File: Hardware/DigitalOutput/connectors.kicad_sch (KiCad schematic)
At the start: 12 parts, among them J1 DIGITAL INPUT, J2 DIGITAL OUTPUT, J3 Conn_02x23_Odd_Even, J4 Conn_02x23_Odd_Even

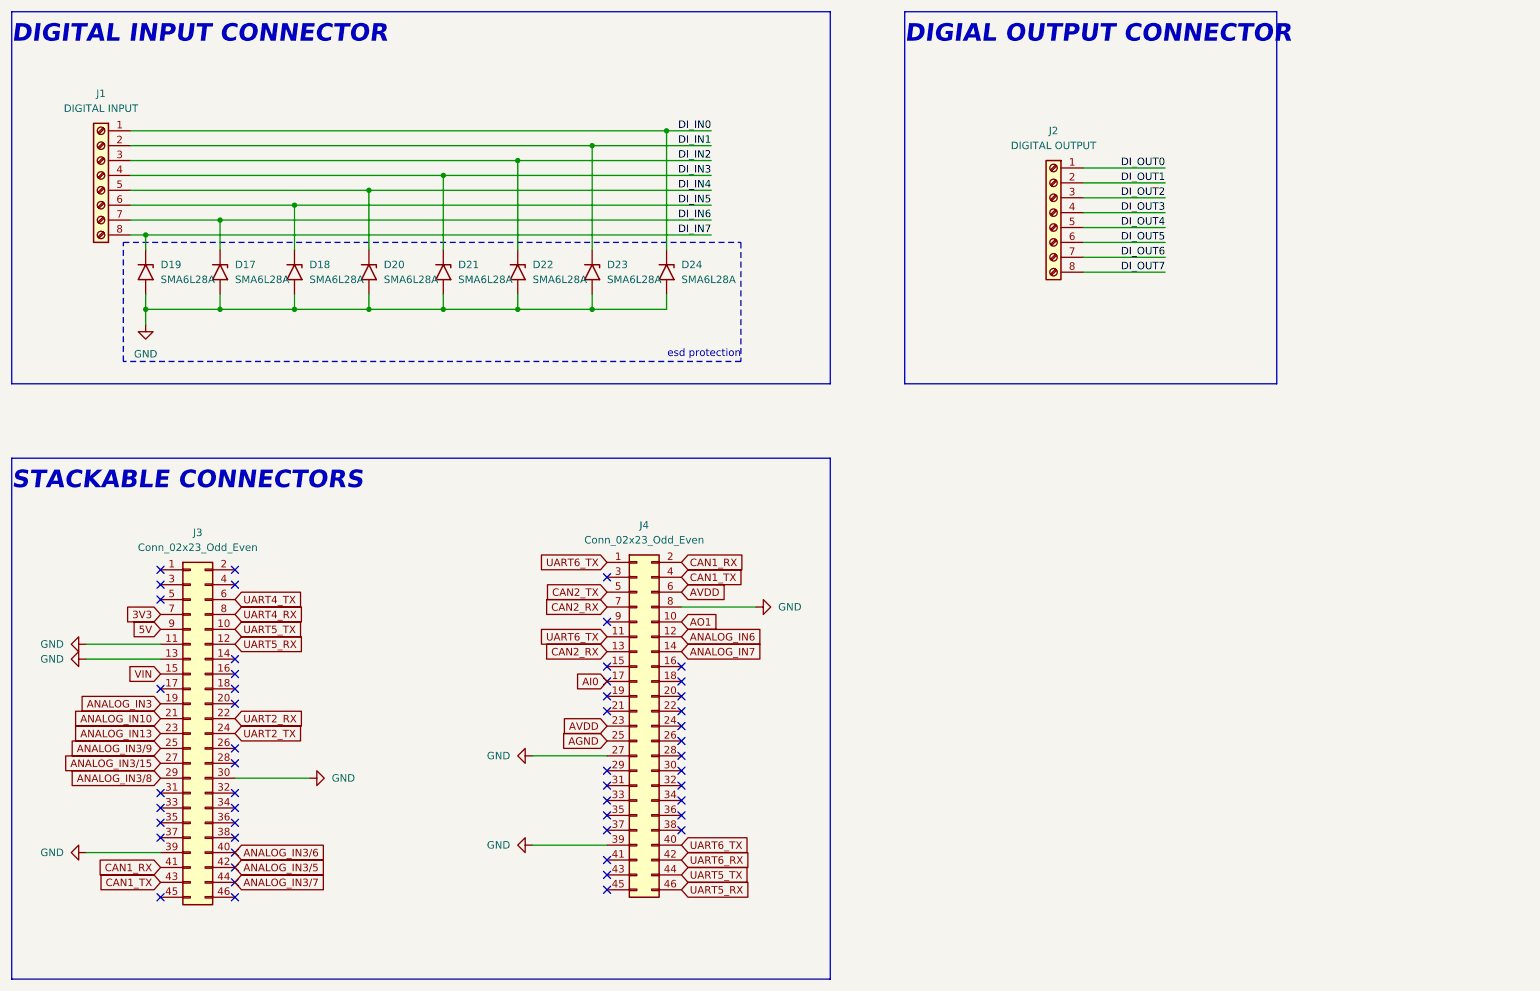
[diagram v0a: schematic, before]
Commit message: digital output & digital input update
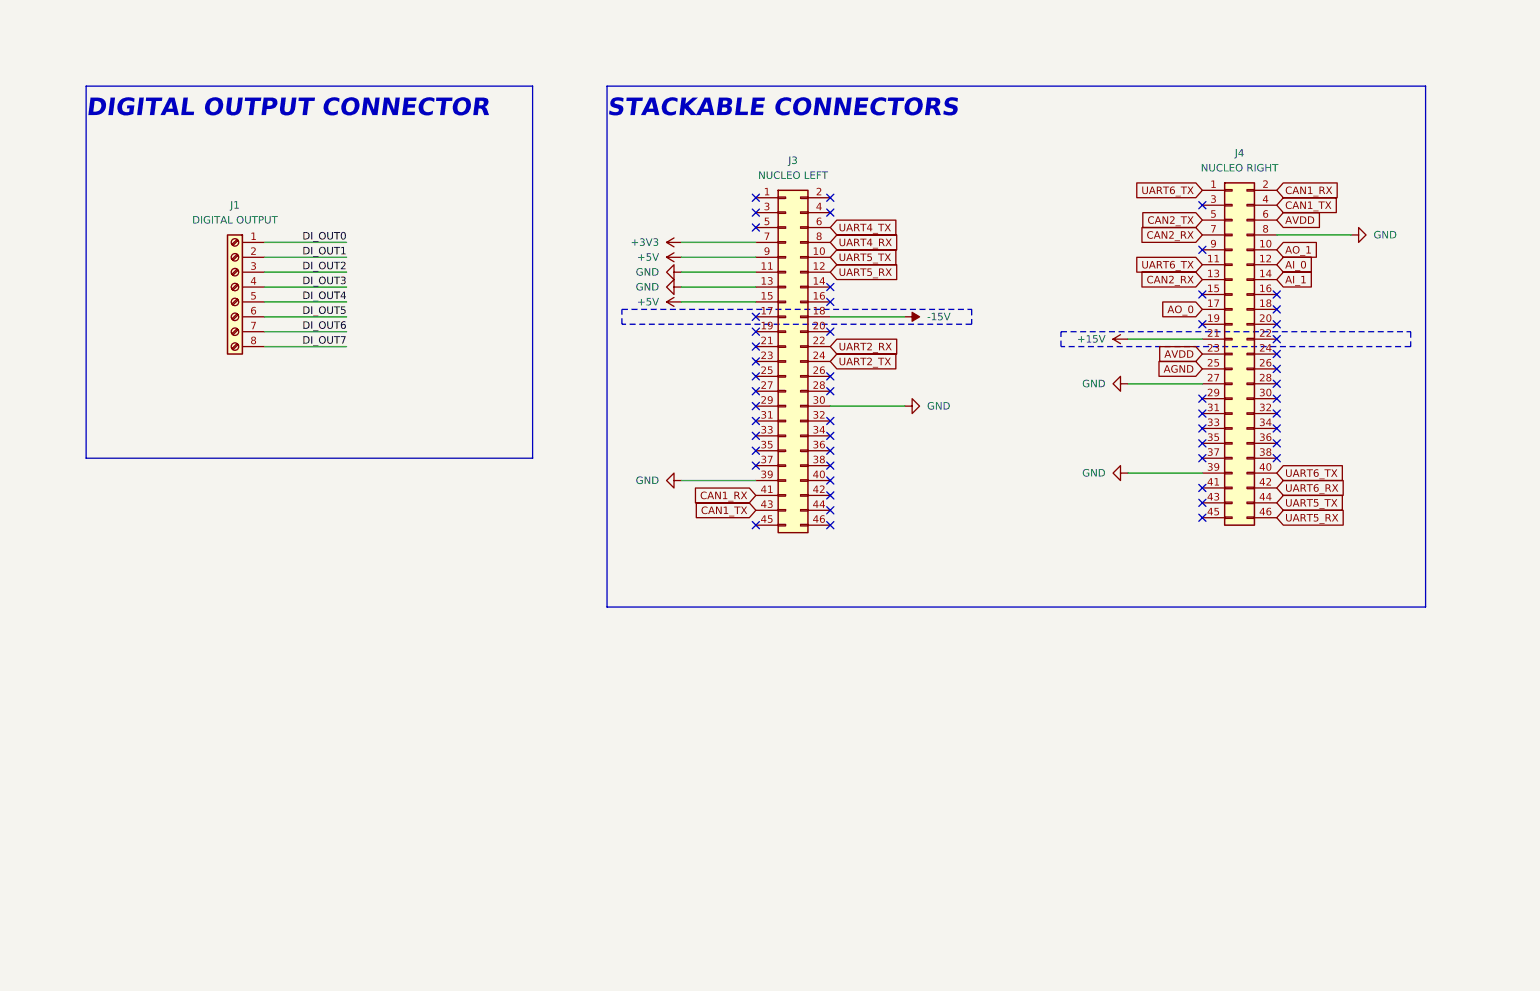
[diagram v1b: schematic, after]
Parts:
- removed D17, D18, D19, D20, D21, D22, D23, D24: SMA6L28A, Diode_SMD:D_SMA, symbol Diode:SMAJ28A
- removed J2: DIGITAL OUTPUT, PLC_STM:1725711, symbol Connector:Screw_Terminal_01x08
- J1: value DIGITAL INPUT -> DIGITAL OUTPUT
- J3: value Conn_02x23_Odd_Even -> NUCLEO LEFT
- J4: value Conn_02x23_Odd_Even -> NUCLEO RIGHT
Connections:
- net DI_IN0 is gone; now on net DI_OUT0: J1.1 (Pin_1)
- net DI_IN1 is gone; now on net DI_OUT1: J1.2 (Pin_2)
- net DI_IN2 is gone; now on net DI_OUT2: J1.3 (Pin_3)
- net DI_IN3 is gone; now on net DI_OUT3: J1.4 (Pin_4)
- net DI_IN4 is gone; now on net DI_OUT4: J1.5 (Pin_5)
- net DI_IN5 is gone; now on net DI_OUT5: J1.6 (Pin_6)
- net DI_IN6 is gone; now on net DI_OUT6: J1.7 (Pin_7)
- net DI_IN7 is gone; now on net DI_OUT7: J1.8 (Pin_8)
- net VIN is gone; now on net +5V: J3.15 (Pin_15)
- net -15V: now reaches J3.18 (Pin_18)
- net +15V: now reaches J4.21 (Pin_21)
- net 3V3 renamed +3V3
- net 5V renamed +5V
- net AI0 renamed AO_0
- net ANALOG_IN10: no longer names the net of J3.21 (Pin_21)
- net ANALOG_IN13: no longer names the net of J3.23 (Pin_23)
- net ANALOG_IN3: no longer names the net of J3.19 (Pin_19)
- net ANALOG_IN3/15: no longer names the net of J3.27 (Pin_27)
- net ANALOG_IN3/5: no longer names the net of J3.42 (Pin_42)
- net ANALOG_IN3/6: no longer names the net of J3.40 (Pin_40)
- net ANALOG_IN3/7: no longer names the net of J3.44 (Pin_44)
- net ANALOG_IN3/8: no longer names the net of J3.29 (Pin_29)
- net ANALOG_IN3/9: no longer names the net of J3.25 (Pin_25)
- net ANALOG_IN6 renamed AI_0
- net ANALOG_IN7 renamed AI_1
- net AO1 renamed AO_1
- no-connect marks 51 -> 54
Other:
- note added: "DIGITAL OUTPUT CONNECTOR"
- note removed: "DIGIAL OUTPUT CONNECTOR"
- note removed: "DIGITAL INPUT CONNECTOR"
- note removed: "esd protection"
- title: PLC on STM - Digital IO Shield -> PLC on STM - Digital Output Shield

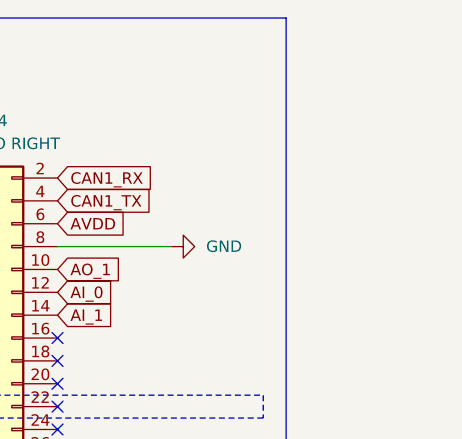
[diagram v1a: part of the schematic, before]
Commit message: digital input finished
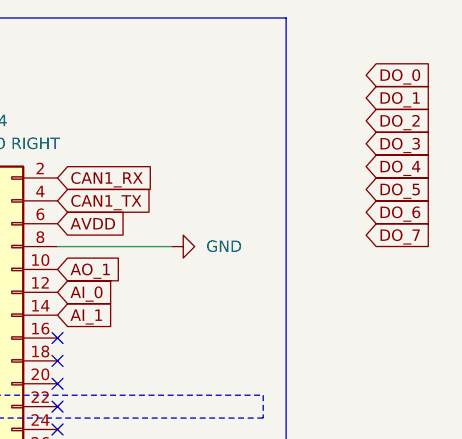
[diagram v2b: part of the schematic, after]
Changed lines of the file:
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@@
+		)
+	)
+	(global_label "DO_0"
+		(shape input)
+		(at 275.59 44.45 0)
+		(fields_autoplaced yes)
+		(effects
+			(font
+				(size 1.27 1.27)
+			)
+			(justify left)
+		)
+		(property "Intersheetrefs" "${INTERSHEET_REFS}"
+			(at 283.3528 44.45 0)
+			(effects
+				(font
+					(size 1.27 1.27)
+				)
+				(justify left)
+				(hide yes)
+			)
 		)
 	)
@@
 		)
 	)
+	(global_label "DO_5"
+		(shape input)
+		(at 275.59 57.15 0)
+		(fields_autoplaced yes)
+		(effects
+			(font
+				(size 1.27 1.27)
+			)
+			(justify left)
+		)
+		(property "Intersheetrefs" "${INTERSHEET_REFS}"
+			(at 283.3528 57.15 0)
+			(effects
+				(font
+					(size 1.27 1.27)
+				)
+				(justify left)
+				(hide yes)
+			)
+		)
+	)
 	(global_label "AI_1"
 		(shape input)
@@
 		)
 	)
+	(global_label "DO_6"
+		(shape input)
+		(at 275.59 59.69 0)
+		(fields_autoplaced yes)
+		(effects
+			(font
+				(size 1.27 1.27)
+			)
+			(justify left)
+		)
+		(property "Intersheetrefs" "${INTERSHEET_REFS}"
+			(at 283.3528 59.69 0)
+			(effects
+				(font
+					(size 1.27 1.27)
+				)
+				(justify left)
+				(hide yes)
+			)
+		)
+	)
 	(global_label "AVDD"
 		(shape input)
@@
 		)
 	)
+	(global_label "DO_7"
+		(shape input)
+		(at 275.59 62.23 0)
+		(fields_autoplaced yes)
+		(effects
+			(font
+				(size 1.27 1.27)
+			)
+			(justify left)
+		)
+		(property "Intersheetrefs" "${INTERSHEET_REFS}"
+			(at 283.3528 62.23 0)
+			(effects
+				(font
+					(size 1.27 1.27)
+				)
+				(justify left)
+				(hide yes)
+			)
+		)
+	)
 	(global_label "AGND"
 		(shape input)
@@
 		)
 	)
+	(global_label "DO_2"
+		(shape input)
+		(at 275.59 49.53 0)
+		(fields_autoplaced yes)
+		(effects
+			(font
+				(size 1.27 1.27)
+			)
+			(justify left)
+		)
+		(property "Intersheetrefs" "${INTERSHEET_REFS}"
+			(at 283.3528 49.53 0)
+			(effects
+				(font
+					(size 1.27 1.27)
+				)
+				(justify left)
+				(hide yes)
+			)
+		)
+	)
 	(global_label "AI_0"
 		(shape input)
@@
 		)
 	)
+	(global_label "DO_4"
+		(shape input)
+		(at 275.59 54.61 0)
+		(fields_autoplaced yes)
+		(effects
+			(font
+				(size 1.27 1.27)
+			)
+			(justify left)
+		)
+		(property "Intersheetrefs" "${INTERSHEET_REFS}"
+			(at 283.3528 54.61 0)
+			(effects
+				(font
+					(size 1.27 1.27)
+				)
+				(justify left)
+				(hide yes)
+			)
+		)
+	)
 	(global_label "CAN2_TX"
 		(shape input)
@@
 				(hide yes)
 			)
+		)
+	)
+	(global_label "DO_3"
+		(shape input)
+		(at 275.59 52.07 0)
+		(fields_autoplaced yes)
+		(effects
+			(font
+				(size 1.27 1.27)
+			)
+			(justify left)
+		)
+		(property "Intersheetrefs" "${INTERSHEET_REFS}"
+			(at 283.3528 52.07 0)
+			(effects
+				(font
+					(size 1.27 1.27)
+				)
+				(justify left)
+				(hide yes)
+			)
+		)
+	)
+	(global_label "DO_1"
+		(shape input)
+		(at 275.59 46.99 0)
+		(fields_autoplaced yes)
+		(effects
+			(font
+				(size 1.27 1.27)
+			)
+			(justify left)
+		)
+		(property "Intersheetrefs" "${INTERSHEET_REFS}"
+			(at 283.3528 46.99 0)
+			(effects
+				(font
+					(size 1.27 1.27)
+				)
+				(justify left)
+				(hide yes)
+			)

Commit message: digital output & power finished
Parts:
- removed J1: DIGITAL OUTPUT, PLC_STM:1725711, symbol Connector:Screw_Terminal_01x08
- added J1: DIGITAL OUTPUT, PLC_STM:1725724, symbol Connector:Screw_Terminal_01x09
- renumbered J3 to J2, J4 to J3
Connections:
- net UART2_RX is gone; now on net GND: J2.22 (Pin_22)
- net UART4_RX is gone; now on net GND: J2.8 (Pin_8)
- net +5V: now also J2.27 (Pin_27); no longer J2.15 (Pin_15), J2.9 (Pin_9)
- net DI_OUT0: now also J1.1 (Pin_1)
- net DI_OUT1: now also J1.2 (Pin_2)
- net DI_OUT2: now also J1.3 (Pin_3)
- net DI_OUT3: now also J1.4 (Pin_4)
- net DI_OUT4: now also J1.5 (Pin_5)
- net DI_OUT5: now also J1.6 (Pin_6)
- net DI_OUT6: now also J1.7 (Pin_7)
- net DI_OUT7: now also J1.8 (Pin_8)
- net DO_0: now also J2.36 (Pin_36)
- net DO_1: now also J2.38 (Pin_38)
- net DO_2: now also J2.40 (Pin_40)
- net DO_3: now also J2.42 (Pin_42)
- net DO_4: now also J3.36 (Pin_36)
- net DO_5: now also J3.34 (Pin_34)
- net DO_6: now also J3.38 (Pin_38)
- net DO_7: now also J3.40 (Pin_40)
- net GND: now also J2.19 (Pin_19), J2.20 (Pin_20), J3.20 (Pin_20), J3.9 (Pin_9); no longer J2.11 (Pin_11), J2.13 (Pin_13), J2.30 (Pin_30), J2.39 (Pin_39), J3.27 (Pin_27), J3.39 (Pin_39), J3.8 (Pin_8)
- net +24V: now reaches J2.29 (Pin_29)
- net +15V: no longer names the net of J3.21 (Pin_21)
- net +3V3: no longer names the net of J2.7 (Pin_7)
- net -15V: no longer names the net of J2.18 (Pin_18)
- net AGND: no longer names the net of J3.25 (Pin_25)
- net AI_0: no longer names the net of J3.12 (Pin_12)
- net AI_1: no longer names the net of J3.14 (Pin_14)
- net AO_0: no longer names the net of J3.17 (Pin_17)
- net AO_1: no longer names the net of J3.10 (Pin_10)
- net AVDD: no longer names the net of J3.23 (Pin_23)
- net AVDD: no longer J3.6 (Pin_6)
- net CAN1_RX: no longer names the net of J3.2 (Pin_2)
- net CAN1_RX: no longer J2.41 (Pin_41)
- net CAN1_TX: no longer names the net of J3.4 (Pin_4)
- net CAN1_TX: no longer J2.43 (Pin_43)
- net CAN2_RX: no longer names the net of J3.13 (Pin_13)
- net CAN2_RX: no longer J3.7 (Pin_7)
- net CAN2_TX: no longer names the net of J3.5 (Pin_5)
- net UART2_TX: no longer names the net of J2.24 (Pin_24)
- net UART4_TX: no longer names the net of J2.6 (Pin_6)
- net UART5_RX: no longer names the net of J3.46 (Pin_46)
- net UART5_RX: no longer J2.12 (Pin_12)
- net UART5_TX: no longer names the net of J3.44 (Pin_44)
- net UART5_TX: no longer J2.10 (Pin_10)
- net UART6_RX: no longer names the net of J3.42 (Pin_42)
- removed net UART6_TX: J3.1 (Pin_1), J3.11 (Pin_11), J3.40 (Pin_40)
- new net GNDREF: J1.9 (Pin_9)
- no-connect marks 54 -> 76
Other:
- note added: "DO LEFT: PC1, PC0, PD3, PG2, PG3, PE2, PE4, PE5 RIGHT: PC4, PF5, PF4, PE8, PF10, PE7, PD14, PF14 DI LEFT: PC2, PC3, PC0, PC1 RIGHT: PC8, PC6, PC5, PB2"

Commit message: small adjustments and final revision
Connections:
- net DO_0: now also J2.40 (Pin_40); no longer J2.36 (Pin_36)
- net DO_1: now also J2.42 (Pin_42); no longer J2.38 (Pin_38)
- net DO_2: now also J2.44 (Pin_44); no longer J2.40 (Pin_40)
- net DO_3: now also J2.46 (Pin_46); no longer J2.42 (Pin_42)
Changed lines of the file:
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@@
-	)
-	(no_connect
-		(at 165.1 110.49)
 	)
 	(no_connect
@@
 	)
 	(no_connect
-		(at 165.1 113.03)
+		(at 165.1 102.87)
 	)
 	(no_connect
@@
 	)
 	(no_connect
+		(at 165.1 100.33)
+	)
+	(no_connect
 		(at 241.3 91.44)
 	)
@@
 		)
 	)
+	(global_label "DO_1"
+		(shape input)
+		(at 165.1 107.95 0)
+		(fields_autoplaced yes)
+		(effects
+			(font
+				(size 1.27 1.27)
+			)
+			(justify left)
+		)
+		(property "Intersheetrefs" "${INTERSHEET_REFS}"
+			(at 172.8628 107.95 0)
+			(effects
+				(font
+					(size 1.27 1.27)
+				)
+				(justify left)
+				(hide yes)
+			)
+		)
+	)
 	(global_label "DI_OUT1"
 		(shape input)
@@
 		)
 	)
+	(global_label "DO_5"
+		(shape input)
+		(at 241.3 96.52 0)
+		(fields_autoplaced yes)
+		(effects
+			(font
+				(size 1.27 1.27)
+			)
+			(justify left)
+		)
+		(property "Intersheetrefs" "${INTERSHEET_REFS}"
+			(at 249.0628 96.52 0)
+			(effects
+				(font
+					(size 1.27 1.27)
+				)
+				(justify left)
+				(hide yes)
+			)
+		)
+	)
 	(global_label "DO_2"
 		(shape input)
+		(at 165.1 110.49 0)
+		(fields_autoplaced yes)
+		(effects
+			(font
+				(size 1.27 1.27)
+			)
+			(justify left)
+		)
+		(property "Intersheetrefs" "${INTERSHEET_REFS}"
+			(at 172.8628 110.49 0)
+			(effects
+				(font
+					(size 1.27 1.27)
+				)
+				(justify left)
+				(hide yes)
+			)
+		)
+	)
+	(global_label "DI_OUT2"
+		(shape input)
+		(at 82.55 69.85 0)
+		(fields_autoplaced yes)
+		(effects
+			(font
+				(size 1.27 1.27)
+			)
+			(justify left)
+		)
+		(property "Intersheetrefs" "${INTERSHEET_REFS}"
+			(at 93.2157 69.85 0)
+			(effects
+				(font
+					(size 1.27 1.27)
+				)
+				(justify left)
+				(hide yes)
+			)
+		)
+	)
+	(global_label "DO_4"
+		(shape input)
+		(at 241.3 99.06 0)
+		(fields_autoplaced yes)
+		(effects
+			(font
+				(size 1.27 1.27)
+			)
+			(justify left)
+		)
+		(property "Intersheetrefs" "${INTERSHEET_REFS}"
+			(at 249.0628 99.06 0)
+			(effects
+				(font
+					(size 1.27 1.27)
+				)
+				(justify left)
+				(hide yes)
+			)
+		)
+	)
+	(global_label "DI_OUT3"
+		(shape input)
+		(at 82.55 72.39 0)
+		(fields_autoplaced yes)
+		(effects
+			(font
+				(size 1.27 1.27)
+			)
+			(justify left)
+		)
+		(property "Intersheetrefs" "${INTERSHEET_REFS}"
+			(at 93.2157 72.39 0)
+			(effects
+				(font
+					(size 1.27 1.27)
+				)
+				(justify left)
+				(hide yes)
+			)
+		)
+	)
+	(global_label "DO_7"
+		(shape input)
+		(at 241.3 104.14 0)
+		(fields_autoplaced yes)
+		(effects
+			(font
+				(size 1.27 1.27)
+			)
+			(justify left)
+		)
+		(property "Intersheetrefs" "${INTERSHEET_REFS}"
+			(at 249.0628 104.14 0)
+			(effects
+				(font
+					(size 1.27 1.27)
+				)
+				(justify left)
+				(hide yes)
+			)
+		)
+	)
+	(global_label "DO_0"
+		(shape input)
 		(at 165.1 105.41 0)
 		(fields_autoplaced yes)
@@
 		)
 	)
-	(global_label "DO_5"
-		(shape input)
-		(at 241.3 96.52 0)
-		(fields_autoplaced yes)
-		(effects
-			(font
-				(size 1.27 1.27)
-			)
-			(justify left)
-		)
-		(property "Intersheetrefs" "${INTERSHEET_REFS}"
-			(at 249.0628 96.52 0)
-			(effects
-				(font
-					(size 1.27 1.27)
-				)
-				(justify left)
-				(hide yes)
-			)
-		)
-	)
-	(global_label "DI_OUT2"
-		(shape input)
-		(at 82.55 69.85 0)
-		(fields_autoplaced yes)
-		(effects
-			(font
-				(size 1.27 1.27)
-			)
-			(justify left)
-		)
-		(property "Intersheetrefs" "${INTERSHEET_REFS}"
-			(at 93.2157 69.85 0)
-			(effects
-				(font
-					(size 1.27 1.27)
-				)
-				(justify left)
-				(hide yes)
-			)
-		)
-	)
-	(global_label "DO_0"
-		(shape input)
-		(at 165.1 100.33 0)
-		(fields_autoplaced yes)
-		(effects
-			(font
-				(size 1.27 1.27)
-			)
-			(justify left)
-		)
-		(property "Intersheetrefs" "${INTERSHEET_REFS}"
-			(at 172.8628 100.33 0)
-			(effects
-				(font
-					(size 1.27 1.27)
-				)
-				(justify left)
-				(hide yes)
-			)
-		)
-	)
-	(global_label "DO_4"
-		(shape input)
-		(at 241.3 99.06 0)
-		(fields_autoplaced yes)
-		(effects
-			(font
-				(size 1.27 1.27)
-			)
-			(justify left)
-		)
-		(property "Intersheetrefs" "${INTERSHEET_REFS}"
-			(at 249.0628 99.06 0)
-			(effects
-				(font
-					(size 1.27 1.27)
-				)
-				(justify left)
-				(hide yes)
-			)
-		)
-	)
-	(global_label "DI_OUT3"
-		(shape input)
-		(at 82.55 72.39 0)
-		(fields_autoplaced yes)
-		(effects
-			(font
-				(size 1.27 1.27)
-			)
-			(justify left)
-		)
-		(property "Intersheetrefs" "${INTERSHEET_REFS}"
-			(at 93.2157 72.39 0)
-			(effects
-				(font
-					(size 1.27 1.27)
-				)
-				(justify left)
-				(hide yes)
-			)
-		)
-	)
-	(global_label "DO_7"
-		(shape input)
-		(at 241.3 104.14 0)
-		(fields_autoplaced yes)
-		(effects
-			(font
-				(size 1.27 1.27)
-			)
-			(justify left)
-		)
-		(property "Intersheetrefs" "${INTERSHEET_REFS}"
-			(at 249.0628 104.14 0)
-			(effects
-				(font
-					(size 1.27 1.27)
-				)
-				(justify left)
-				(hide yes)
-			)
-		)
-	)
 	(global_label "DI_OUT0"
 		(shape input)
@@
 	(global_label "DO_3"
 		(shape input)
-		(at 165.1 107.95 0)
-		(fields_autoplaced yes)
-		(effects
-			(font
-				(size 1.27 1.27)
-			)
-			(justify left)
-		)
-		(property "Intersheetrefs" "${INTERSHEET_REFS}"
-			(at 172.8628 107.95 0)
+		(at 165.1 113.03 0)
+		(fields_autoplaced yes)
+		(effects
+			(font
+				(size 1.27 1.27)
+			)
+			(justify left)
+		)
+		(property "Intersheetrefs" "${INTERSHEET_REFS}"
+			(at 172.8628 113.03 0)
 			(effects
 				(font
@@
 			(effects
 				(font
-					(size 1.27 1.27)
-				)
-				(justify left)
-				(hide yes)
-			)
-		)
-	)
-	(global_label "DO_1"
-		(shape input)
-		(at 165.1 102.87 0)
-		(fields_autoplaced yes)
-		(effects
-			(font
-				(size 1.27 1.27)
-			)
-			(justify left)
-		)
-		(property "Intersheetrefs" "${INTERSHEET_REFS}"
-			(at 172.8628 102.87 0)
-			(effects
-				(font
